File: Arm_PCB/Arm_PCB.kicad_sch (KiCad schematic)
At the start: 10 parts

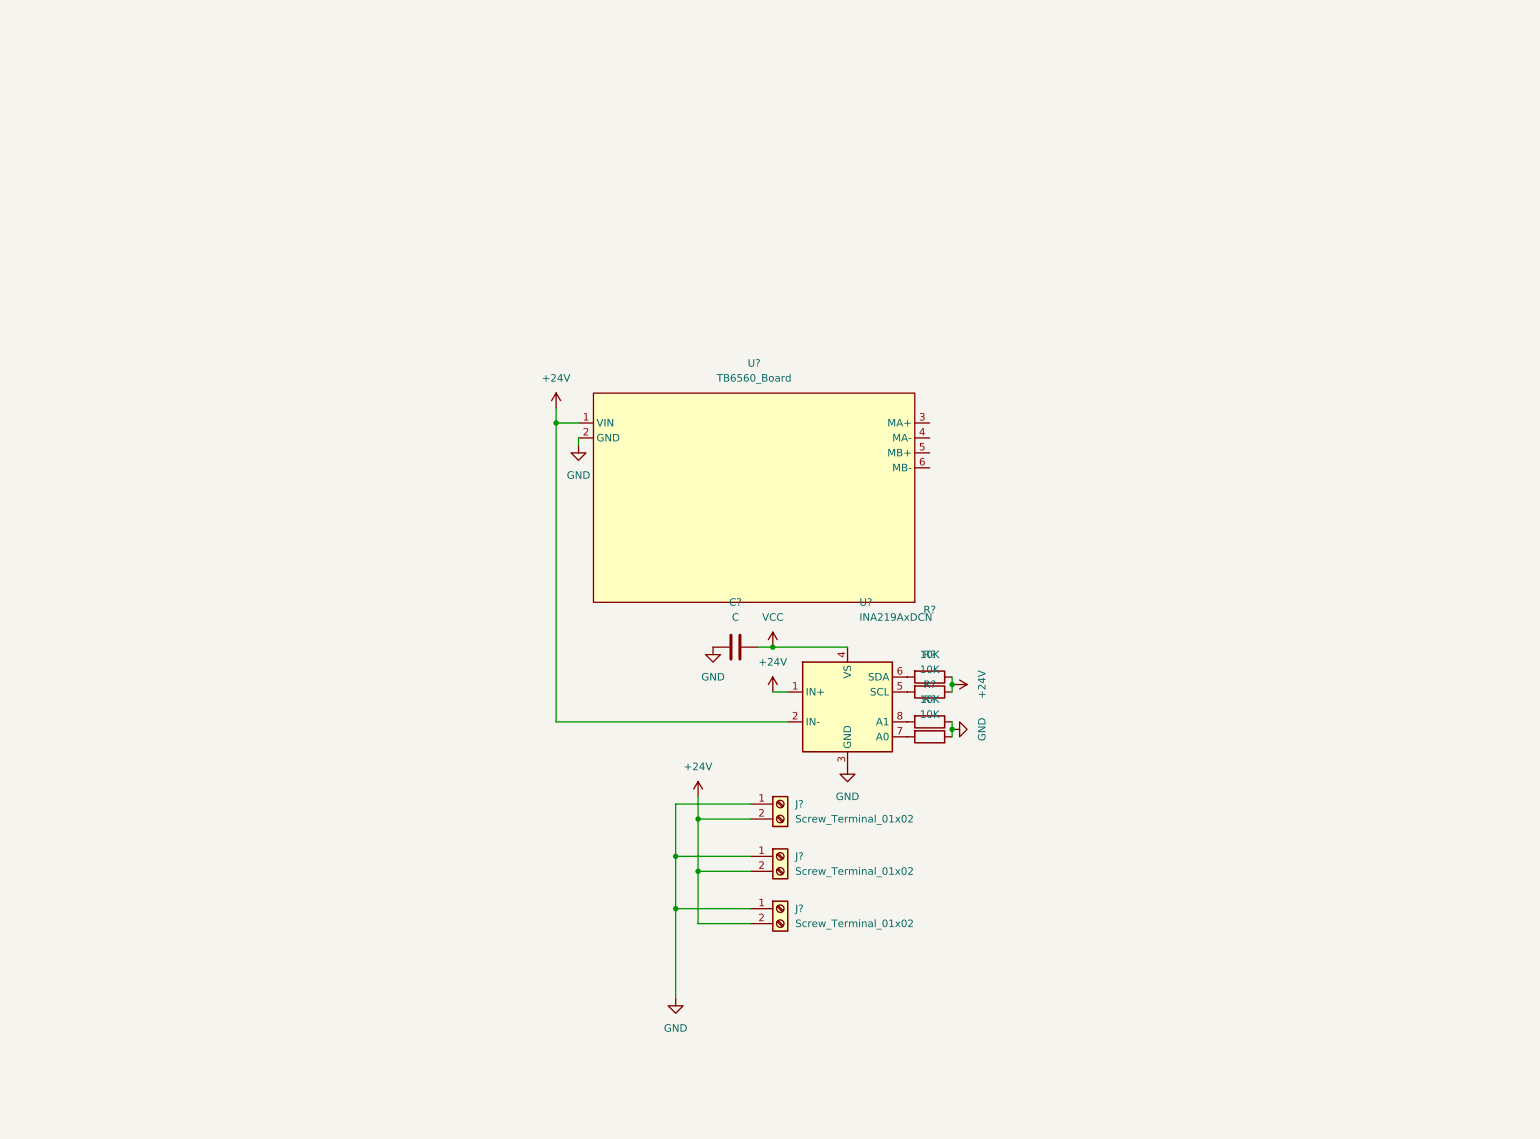
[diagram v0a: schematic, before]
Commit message: Added motor controllers and the micro-controllers"
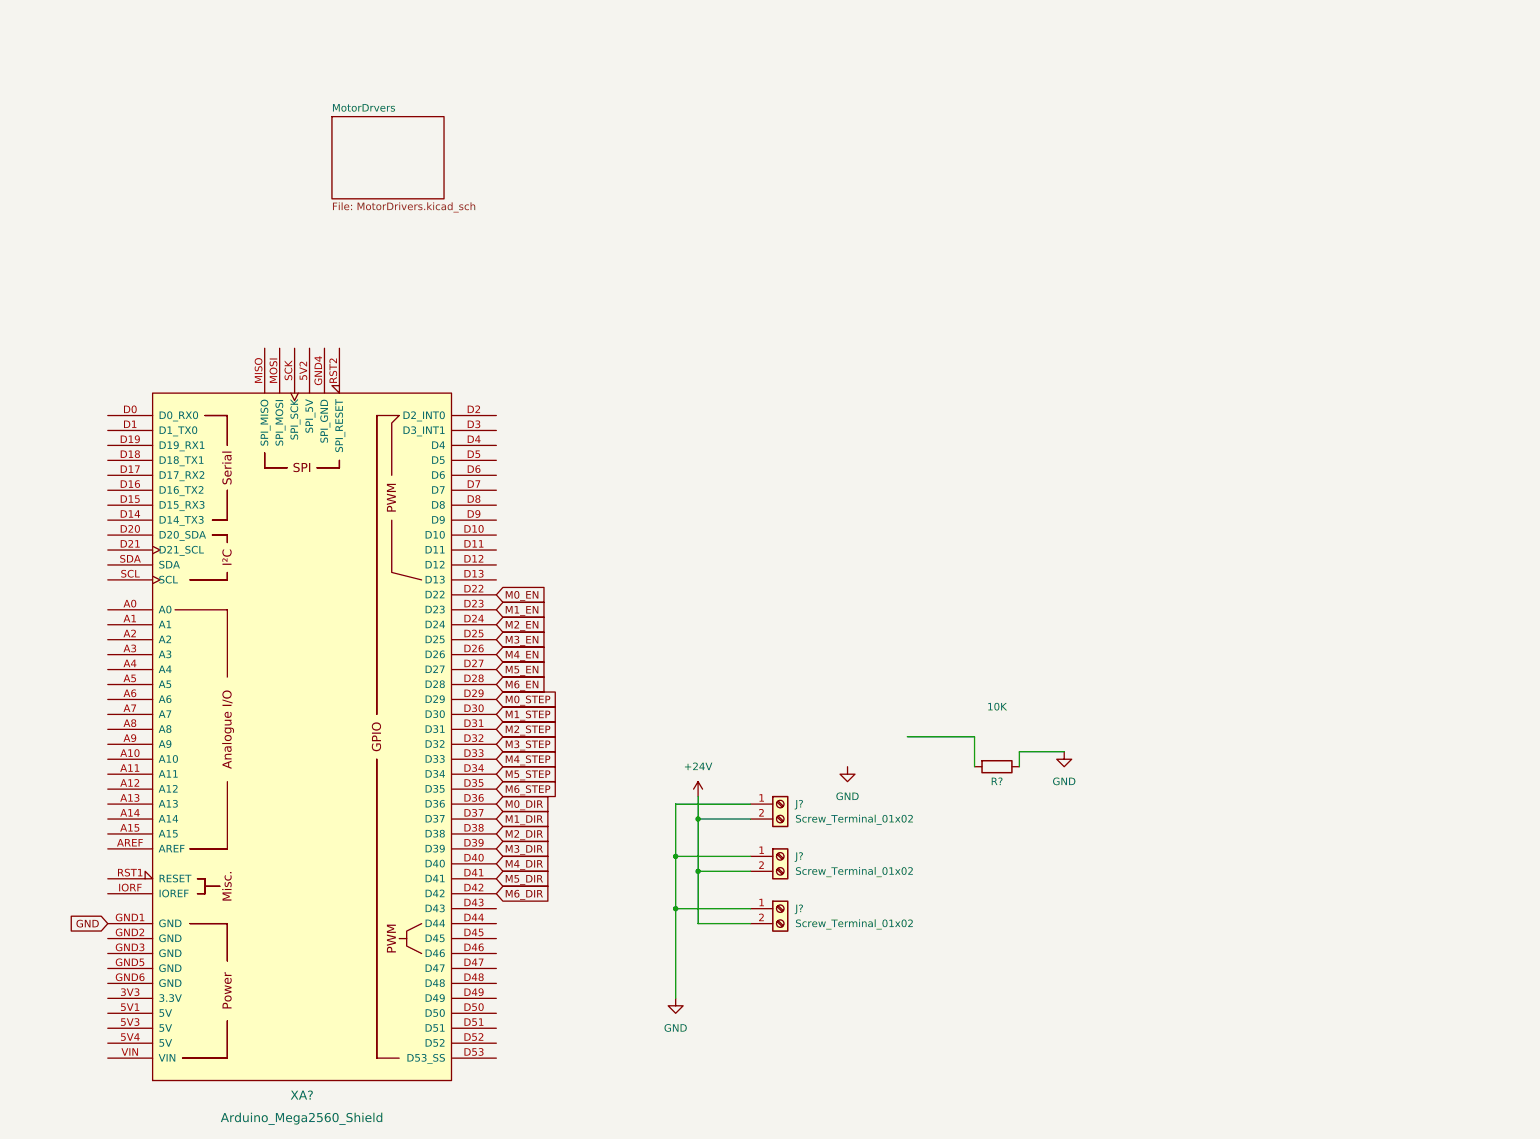
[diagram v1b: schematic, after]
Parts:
- removed C?: C, symbol Device:C
- removed R? (x3): 10K, symbol Device:R
- removed U?: INA219AxDCN, Package_TO_SOT_SMD:SOT-23-8, symbol Sensor_Energy:INA219AxDCN
- removed U?: TB6560_Board, symbol SSRT_Arm_Library:TB6560_Board
- added XA?: Arduino_Mega2560_Shield, Arduino_Library:Arduino_Mega2560_Shield, symbol Arduino_Library:Arduino_Mega2560_Shield
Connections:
- net GND: now also XA?.GND1 (GND)
- new net M0_DIR: XA?.D36
- new net M0_EN: XA?.D22
- new net M0_STEP: XA?.D29
- new net M1_DIR: XA?.D37
- new net M1_EN: XA?.D23
- new net M1_STEP: XA?.D30
- new net M2_DIR: XA?.D38
- new net M2_EN: XA?.D24
- new net M2_STEP: XA?.D31
- new net M3_DIR: XA?.D39
- new net M3_EN: XA?.D25
- new net M3_STEP: XA?.D32
- new net M4_DIR: XA?.D40
- new net M4_EN: XA?.D26
- new net M4_STEP: XA?.D33
- new net M5_DIR: XA?.D41
- new net M5_EN: XA?.D27
- new net M5_STEP: XA?.D34
- new net M6_DIR: XA?.D42
- new net M6_EN: XA?.D28
- new net M6_STEP: XA?.D35
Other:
- added sheet MotorDrvers (MotorDrivers.kicad_sch)
- moved on the sheet: R?

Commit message: Added the INA219 schematics,fixed the TB6560 board, added LED for the EN pin on the microcontroller
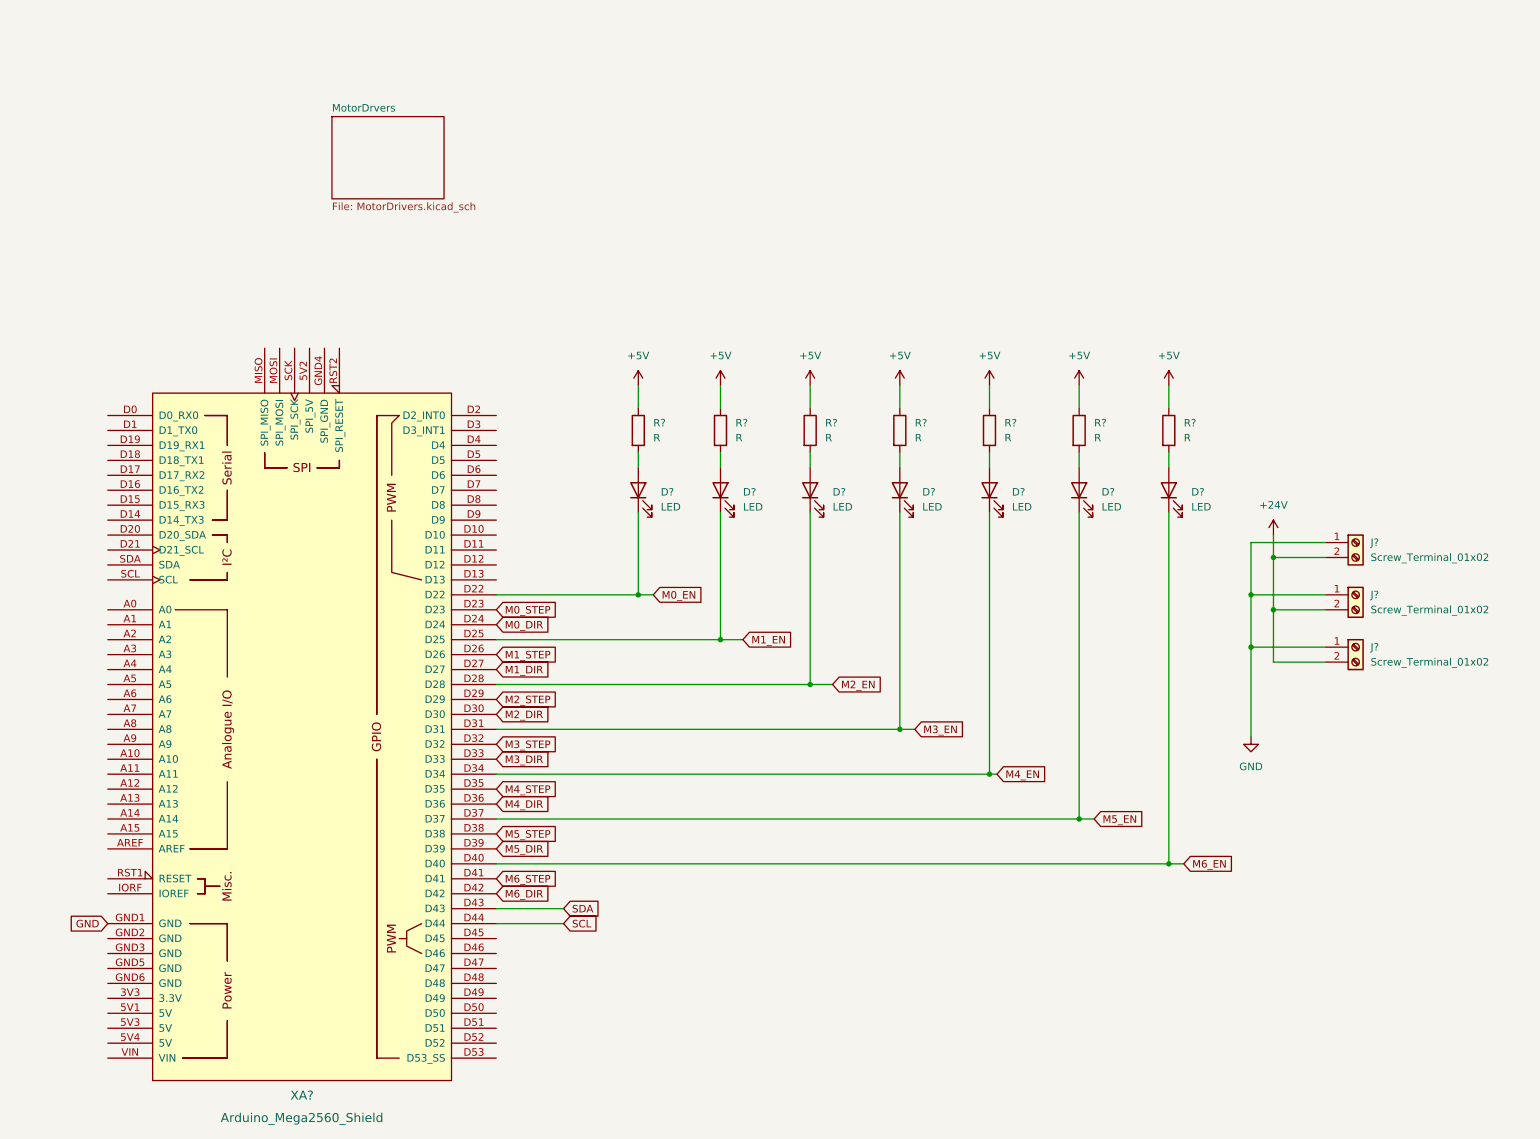
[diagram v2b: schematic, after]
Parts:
- removed R?: 10K, symbol Device:R
- added D? (x7): LED, symbol Device:LED
- added R? (x7): R, symbol Device:R
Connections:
- net M0_DIR: now also XA?.D24; no longer XA?.D36
- net M0_EN: now also D?.1 (K)
- net M0_STEP: now also XA?.D23; no longer XA?.D29
- net M1_DIR: now also XA?.D27; no longer XA?.D37
- net M1_EN: now also XA?.D25, D?.1 (K); no longer XA?.D23
- net M1_STEP: now also XA?.D26; no longer XA?.D30
- net M2_DIR: now also XA?.D30; no longer XA?.D38
- net M2_EN: now also XA?.D28, D?.1 (K); no longer XA?.D24
- net M2_STEP: now also XA?.D29; no longer XA?.D31
- net M3_DIR: now also XA?.D33; no longer XA?.D39
- net M3_EN: now also XA?.D31, D?.1 (K); no longer XA?.D25
- net M4_DIR: now also XA?.D36; no longer XA?.D40
- net M4_EN: now also XA?.D34, D?.1 (K); no longer XA?.D26
- net M4_STEP: now also XA?.D35; no longer XA?.D33
- net M5_DIR: now also XA?.D39; no longer XA?.D41
- net M5_EN: now also XA?.D37, D?.1 (K); no longer XA?.D27
- net M5_STEP: now also XA?.D38; no longer XA?.D34
- net M6_EN: now also XA?.D40, D?.1 (K); no longer XA?.D28
- net M6_STEP: now also XA?.D41; no longer XA?.D35
- net SDA: now reaches XA?.D43
- net SCL: now reaches XA?.D44
- new net: D?.2 (A), R?.2 (x7)
- new net +5V: R?.1, R?.1, R?.1, R?.1, R?.1, R?.1, R?.1
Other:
- moved on the sheet: J?

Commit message: Changes
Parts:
- added J? (x4): Screw_Terminal_01x02, symbol Connector:Screw_Terminal_01x02
- added JP? (x2): Jumper_2_Open, symbol Jumper:Jumper_2_Open
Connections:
- net +24V: now also JP?.1 (A)
- net +5V: now also J?.2 (Pin_2), J?.2 (Pin_2), JP?.1 (A)
- net GND: now also XA?.GND2 (GND), XA?.GND3 (GND), XA?.GND5 (GND), XA?.GND6 (GND); no longer J?.1 (Pin_1), J?.1 (Pin_1), J?.1 (Pin_1)
- net at XA?.5V1 (5V): now also XA?.5V3 (5V), XA?.5V4 (5V), JP?.2 (B)
- net at XA?.VIN: now also JP?.2 (B)
- new net +3.3V: J?.2 (Pin_2), J?.2 (Pin_2)
- new net GNDPWR: J?.1 (Pin_1), J?.1 (Pin_1), J?.1 (Pin_1), J?.1 (Pin_1), J?.1 (Pin_1), J?.1 (Pin_1), J?.1 (Pin_1)
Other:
- sheet MotorDrvers renamed MotorDrivers
- added sheet UXElements (UXElements.kicad_sch)
- note added: "Enable LEDs (EN is Active-Low, LEDs on when EN)"
- note added: "Exposed Power Terminals"
- note added: "Power Input Terminals"
